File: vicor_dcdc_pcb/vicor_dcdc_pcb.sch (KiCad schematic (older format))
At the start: 6 parts, among them P1 CONN_01X02_2XMNT, P2 CONN_01X04-2XMNT, U1 VICOR-DCDC

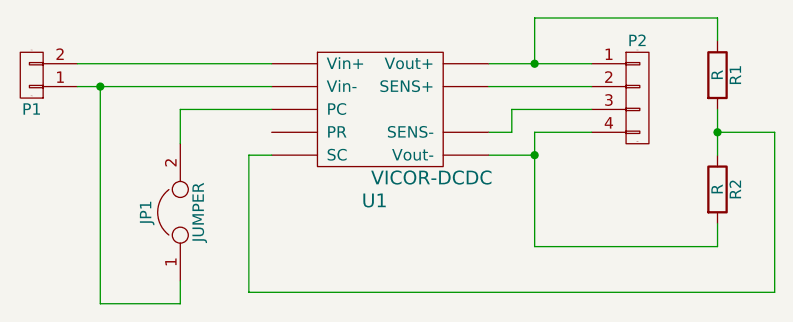
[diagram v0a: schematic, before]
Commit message: small changes to vicor dcdc pcb
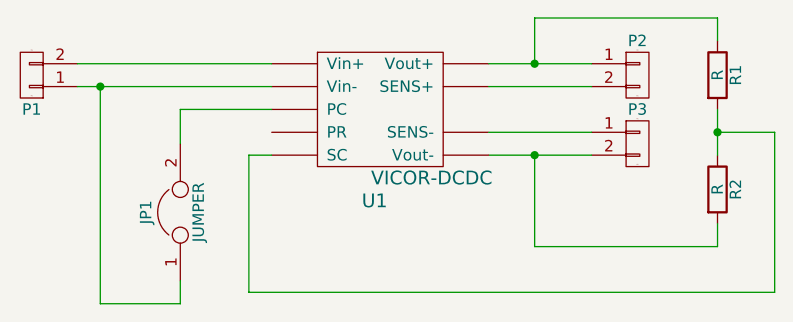
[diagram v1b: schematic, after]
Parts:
- removed P2: CONN_01X04-2XMNT, -footprints:CONN-TE-MICROMNL-4-PTH-MALE-RGT, symbol CONN_01X04-2XMNT
- added P2, P3: CONN_01X02_2XMNT, -footprints:CONN-TE-MICROMNL-2-PTH-MALE-RGT, symbol CONN_01X02_2XMNT
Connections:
- net at R2.2, U1.5 (Vout-): now also P3.2 (P2)
- net at U1.6 (SENS-): now also P3.1 (P1)
- net at U1.8 (SENS+): now also P2.2 (P2)
- net at R1.1, U1.9 (Vout+): now also P2.1 (P1)
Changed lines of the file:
@@
-	1    0    0    -1
-$EndComp
-$Comp
-L CONN_01X04-2XMNT P2
-U 1 1 5739782B
-P 5300 1800
-F 0 "P2" H 5300 2050 50  0000 C CNN
-F 1 "CONN_01X04-2XMNT" V 5400 1800 50  0001 C CNN
-F 2 "-footprints:CONN-TE-MICROMNL-4-PTH-MALE-RGT" H 5300 1800 50  0001 C CNN
-F 3 "" H 5300 1800 50  0000 C CNN
-	1    5300 1800
 	1    0    0    -1
 $EndComp
@@
 	4650 1750 5100 1750
 Wire Wire Line
-	4650 1950 4750 1950
+	4650 1950 5100 1950
 Wire Wire Line
-	4750 1950 4750 1850
+	4650 2050 5100 2050
 Wire Wire Line
-	4750 1850 5100 1850
-Wire Wire Line
-	4650 2050 4850 2050
-Wire Wire Line
-	4850 1950 4850 2450
-Wire Wire Line
-	4850 1950 5100 1950
+	4850 2050 4850 2450
 $Comp
 L R R1
@@
 Connection ~ 4850 2050
 Wire Wire Line
-	5650 2050 5650 1850
+	5650 1850 5650 2050
 Wire Wire Line
 	5650 1550 5650 1450
@@
 Wire Wire Line
 	3700 1650 2850 1650
+$Comp
+L CONN_01X02_2XMNT P2
+U 1 1 573983E3
+P 5300 1700
+F 0 "P2" H 5300 1850 50  0000 C CNN
+F 1 "CONN_01X02_2XMNT" V 5400 1700 50  0001 C CNN
+F 2 "-footprints:CONN-TE-MICROMNL-2-PTH-MALE-RGT" H 5300 1700 50  0001 C CNN
+F 3 "" H 5300 1700 50  0000 C CNN
+	1    5300 1700
+	1    0    0    -1
+$EndComp
+$Comp
+L CONN_01X02_2XMNT P3
+U 1 1 5739858A
+P 5300 2000
+F 0 "P3" H 5300 2150 50  0000 C CNN
+F 1 "CONN_01X02_2XMNT" V 5400 2000 50  0001 C CNN
+F 2 "-footprints:CONN-TE-MICROMNL-2-PTH-MALE-RGT" H 5300 2000 50  0001 C CNN
+F 3 "" H 5300 2000 50  0000 C CNN
+	1    5300 2000
+	1    0    0    -1
+$EndComp
 $EndSCHEMATC
